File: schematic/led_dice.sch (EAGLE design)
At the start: 14 parts, among them U1 ATTINY85-20P, X1 332-02

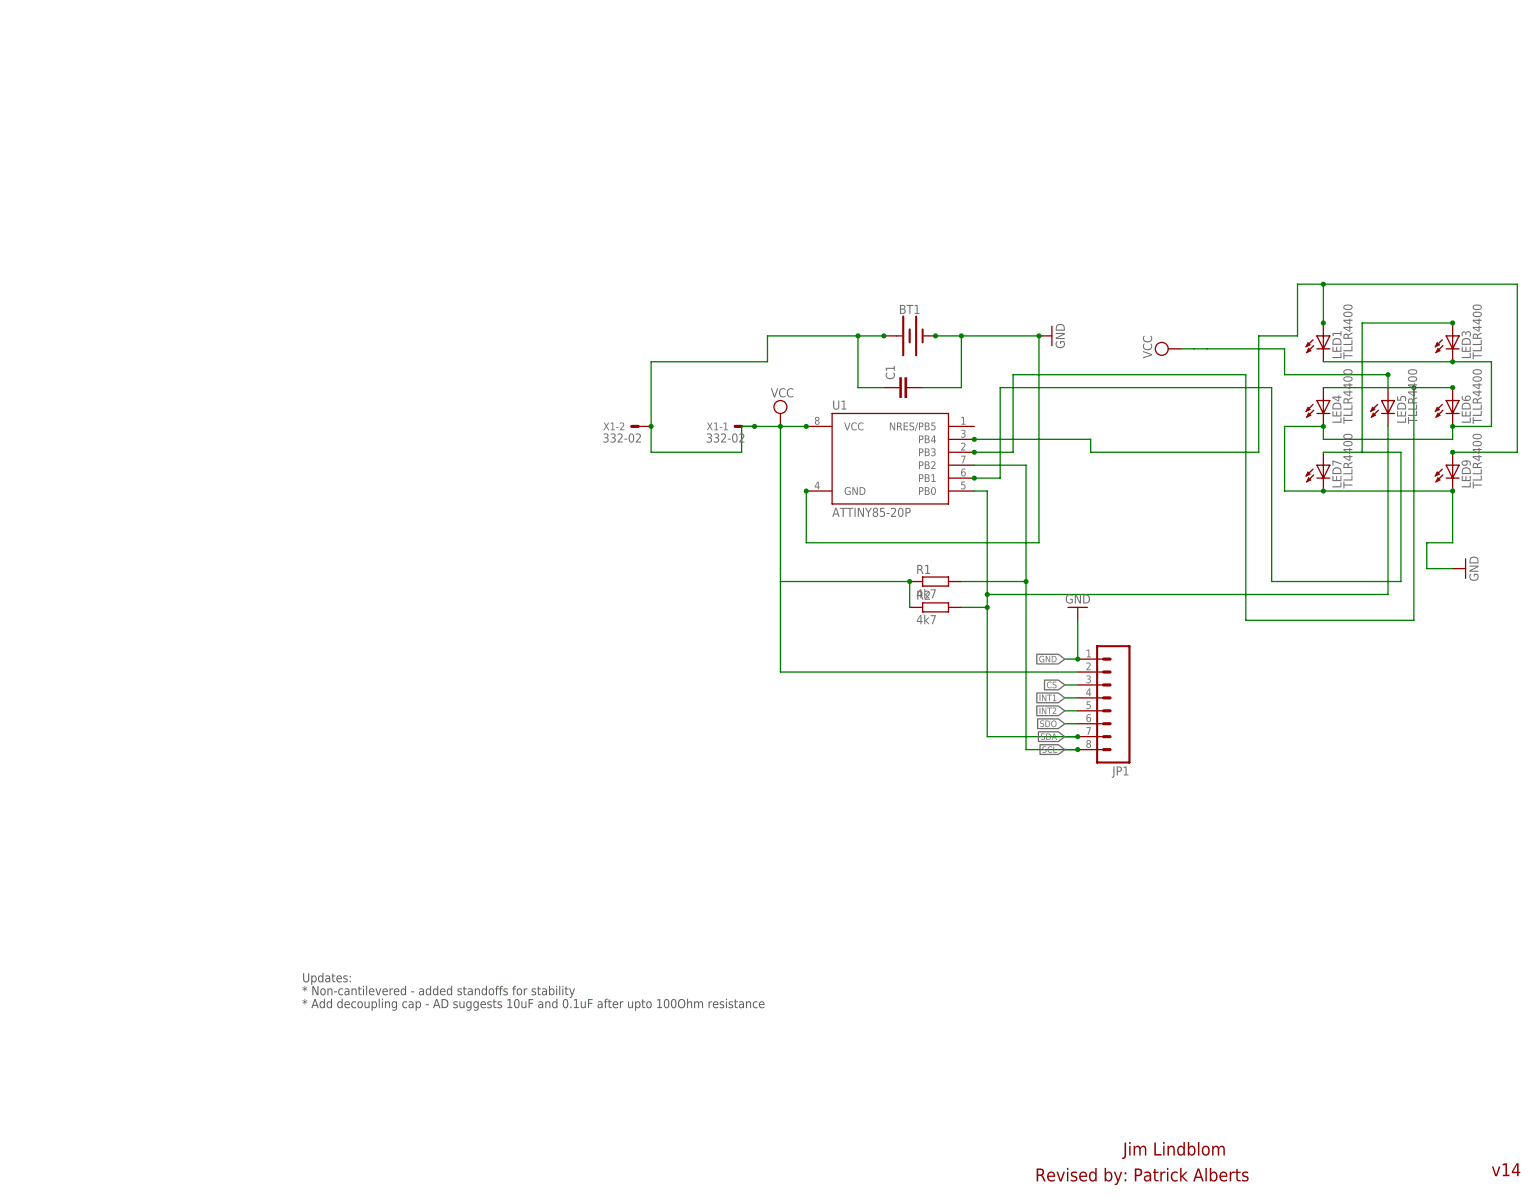
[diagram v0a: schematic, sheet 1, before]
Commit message: ADXL345 Shake detection added to Sketch + Schematic updated
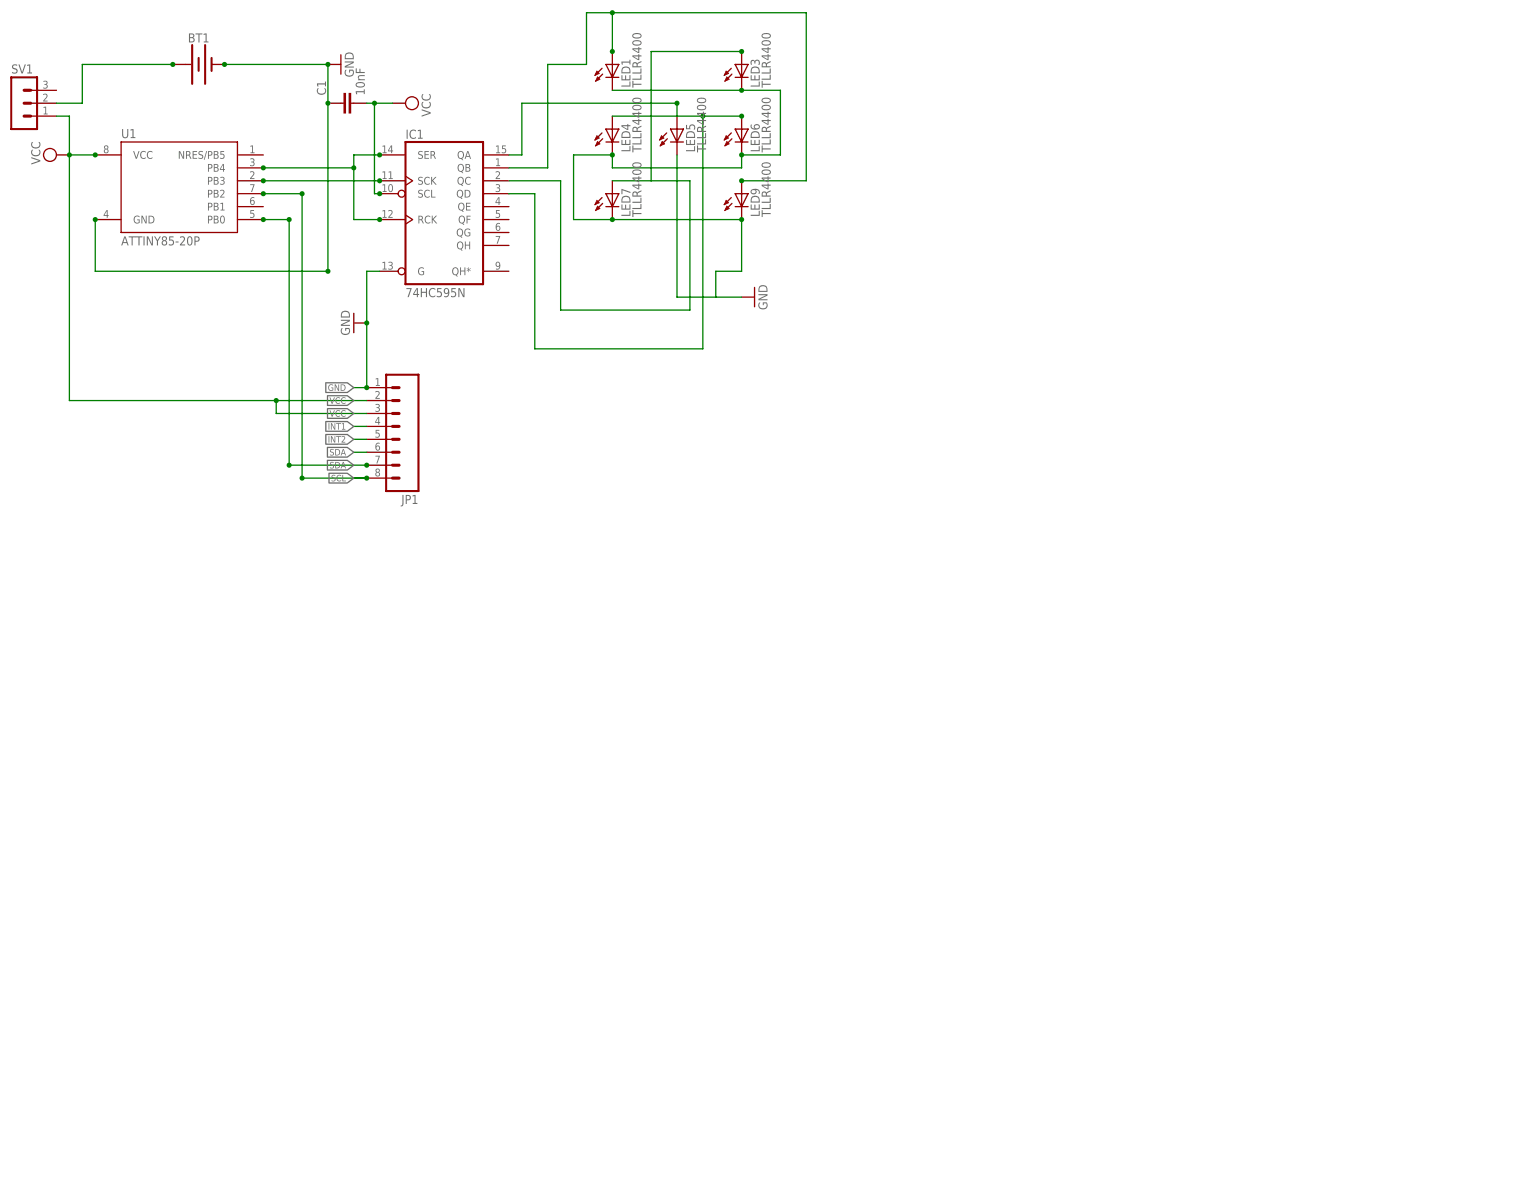
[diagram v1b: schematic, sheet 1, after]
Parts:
- removed R1: 4k7, resistor:R-EU_0207/12
- removed R2: 4k7, resistor:R-EU_0207/2V
- removed X1: 332-02, con-garry:332-02
- added IC1: 74HC595N, 74xx-eu:74HC595N
- added SV1: (no value), con-lstb:MA03-1
- C1: value (none) -> 10nF
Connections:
- net SDO renamed N$10
- removed net CS: JP1.3
- new net N$3: IC1A.QA, LED5.A
- new net N$4: IC1A.SCK, U1.PB3
- new net N$6: BT1.+, SV1.2
- new net N$8: IC1A.RCK, IC1A.SER, U1.PB4
- net GND: now also C1.1, IC1A.G, LED5.C; no longer C1.2
- net N$2: now also IC1A.QB; no longer U1.PB4
- net N$5: now also IC1A.QD; no longer U1.PB3
- net N$7: now also IC1A.QC; no longer U1.PB1
- net SCL: no longer R1.2
- net SDA: no longer LED5.C, R2.2
- net VCC: now also C1.2, IC1A.SCL, JP1.3, SV1.1; no longer BT1.+, C1.1, LED5.A, R1.1, R2.1, X1-1.S, X1-2.S
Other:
- note removed: "* Add decoupling cap - AD suggests 10uF and 0.1uF after upto 100Ohm resistance"
- note removed: "* Non-cantilevered - added standoffs for stability"
- note removed: "Jim Lindblom"
- note removed: "Revised by: Patrick Alberts"
- note removed: "Updates:"
- note removed: "v14"
- moved on the sheet: BT1, C1, JP1, LED1, LED3, LED4, LED5, LED6, LED7, LED9, U1

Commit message: Sketch: added Shuffle Effect + 3d case updated
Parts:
- renumbered JP1 to ADXL345
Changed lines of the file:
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@@
 <part name="GND1" library="supply1" deviceset="GND" device=""/>
 <part name="GND2" library="SparkFun" deviceset="GND" device=""/>
-<part name="JP1" library="SparkFun" deviceset="M08" device=""/>
+<part name="ADXL345" library="SparkFun" deviceset="M08" device=""/>
 <part name="GND4" library="SparkFun" deviceset="GND" device=""/>
 <part name="C1" library="resistor" library_urn="urn:adsk.eagle:library:348" deviceset="C-EU" device="025-024X044" package3d_urn="urn:adsk.eagle:package:26149/1" value="10nF"/>
@@
 <attribute name="VALUE" x="35.56" y="5.08" size="1.778" layer="96" rot="R270"/>
 </instance>
-<instance part="JP1" gate="G$1" x="45.72" y="-17.78" smashed="yes" rot="R180">
+<instance part="ADXL345" gate="G$1" x="45.72" y="-17.78" smashed="yes" rot="R180">
 <attribute name="VALUE" x="50.8" y="-5.08" size="1.778" layer="96" rot="R180"/>
 <attribute name="NAME" x="50.8" y="-31.242" size="1.778" layer="95" rot="R180"/>
@@
 <pinref part="GND2" gate="1" pin="GND"/>
 <wire x1="40.64" y1="-10.16" x2="38.1" y2="-10.16" width="0.1524" layer="91"/>
-<pinref part="JP1" gate="G$1" pin="1"/>
+<pinref part="ADXL345" gate="G$1" pin="1"/>
 <label x="38.1" y="-10.16" size="1.27" layer="95" rot="R180" xref="yes"/>
 <wire x1="40.64" y1="2.54" x2="40.64" y2="-10.16" width="0.1524" layer="91"/>
@@
 <segment>
 <wire x1="40.64" y1="-20.32" x2="38.1" y2="-20.32" width="0.1524" layer="91"/>
-<pinref part="JP1" gate="G$1" pin="5"/>
+<pinref part="ADXL345" gate="G$1" pin="5"/>
 <label x="38.1" y="-20.32" size="1.27" layer="95" rot="R180" xref="yes"/>
 </segment>
@@
 <segment>
 <wire x1="40.64" y1="-17.78" x2="38.1" y2="-17.78" width="0.1524" layer="91"/>
-<pinref part="JP1" gate="G$1" pin="4"/>
+<pinref part="ADXL345" gate="G$1" pin="4"/>
 <label x="38.1" y="-17.78" size="1.27" layer="95" rot="R180" xref="yes"/>
 </segment>
@@
 <pinref part="SV1" gate="G$1" pin="1"/>
 <wire x1="-20.32" y1="43.18" x2="-17.78" y2="43.18" width="0.1524" layer="91"/>
-<pinref part="JP1" gate="G$1" pin="2"/>
+<pinref part="ADXL345" gate="G$1" pin="2"/>
 <wire x1="40.64" y1="-12.7" x2="22.86" y2="-12.7" width="0.1524" layer="91"/>
 <wire x1="22.86" y1="-12.7" x2="-17.78" y2="-12.7" width="0.1524" layer="91"/>
 <wire x1="-17.78" y1="-12.7" x2="-17.78" y2="35.56" width="0.1524" layer="91"/>
 <label x="38.1" y="-12.7" size="1.27" layer="95" rot="R180" xref="yes"/>
-<pinref part="JP1" gate="G$1" pin="3"/>
+<pinref part="ADXL345" gate="G$1" pin="3"/>
 <label x="38.1" y="-15.24" size="1.27" layer="95" rot="R180" xref="yes"/>
 <wire x1="40.64" y1="-15.24" x2="22.86" y2="-15.24" width="0.1524" layer="91"/>
@@
 <segment>
 <wire x1="40.64" y1="-27.94" x2="38.1" y2="-27.94" width="0.1524" layer="91"/>
-<pinref part="JP1" gate="G$1" pin="8"/>
+<pinref part="ADXL345" gate="G$1" pin="8"/>
 <label x="38.1" y="-27.94" size="1.27" layer="95" rot="R180" xref="yes"/>
 <wire x1="40.64" y1="-27.94" x2="27.94" y2="-27.94" width="0.1524" layer="91"/>
@@
 <net name="SDA" class="0">
 <segment>
-<pinref part="JP1" gate="G$1" pin="7"/>
+<pinref part="ADXL345" gate="G$1" pin="7"/>
 <label x="38.1" y="-22.86" size="1.27" layer="95" rot="R180" xref="yes"/>
 <label x="38.1" y="-25.4" size="1.27" layer="95" rot="R180" xref="yes"/>
@@
 <net name="N$10" class="0">
 <segment>
-<pinref part="JP1" gate="G$1" pin="6"/>
+<pinref part="ADXL345" gate="G$1" pin="6"/>
 <wire x1="40.64" y1="-22.86" x2="38.1" y2="-22.86" width="0.1524" layer="91"/>
 </segment>
